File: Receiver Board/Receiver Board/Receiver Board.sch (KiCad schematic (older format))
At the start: 18 parts

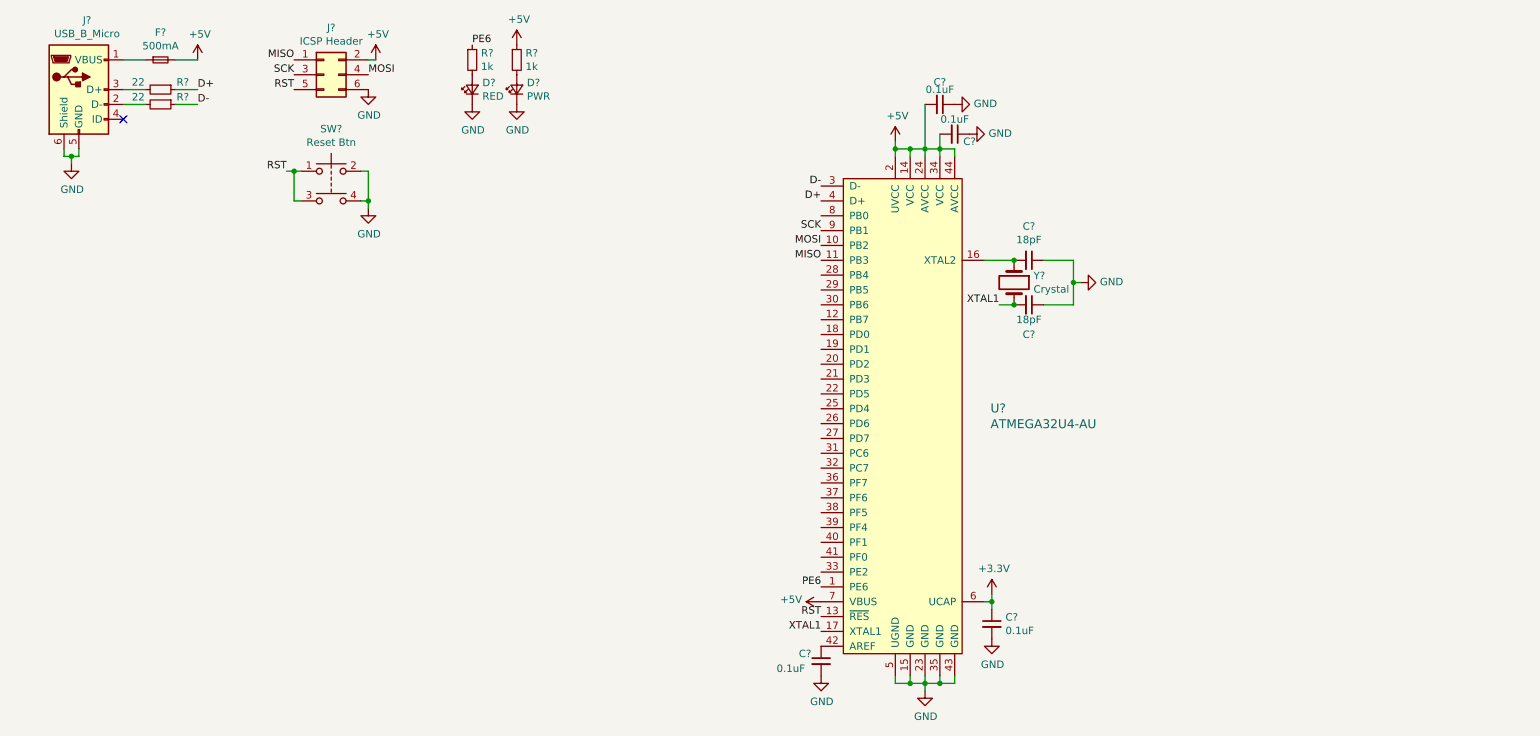
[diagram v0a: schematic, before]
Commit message: Receiver Board Schematic Complete
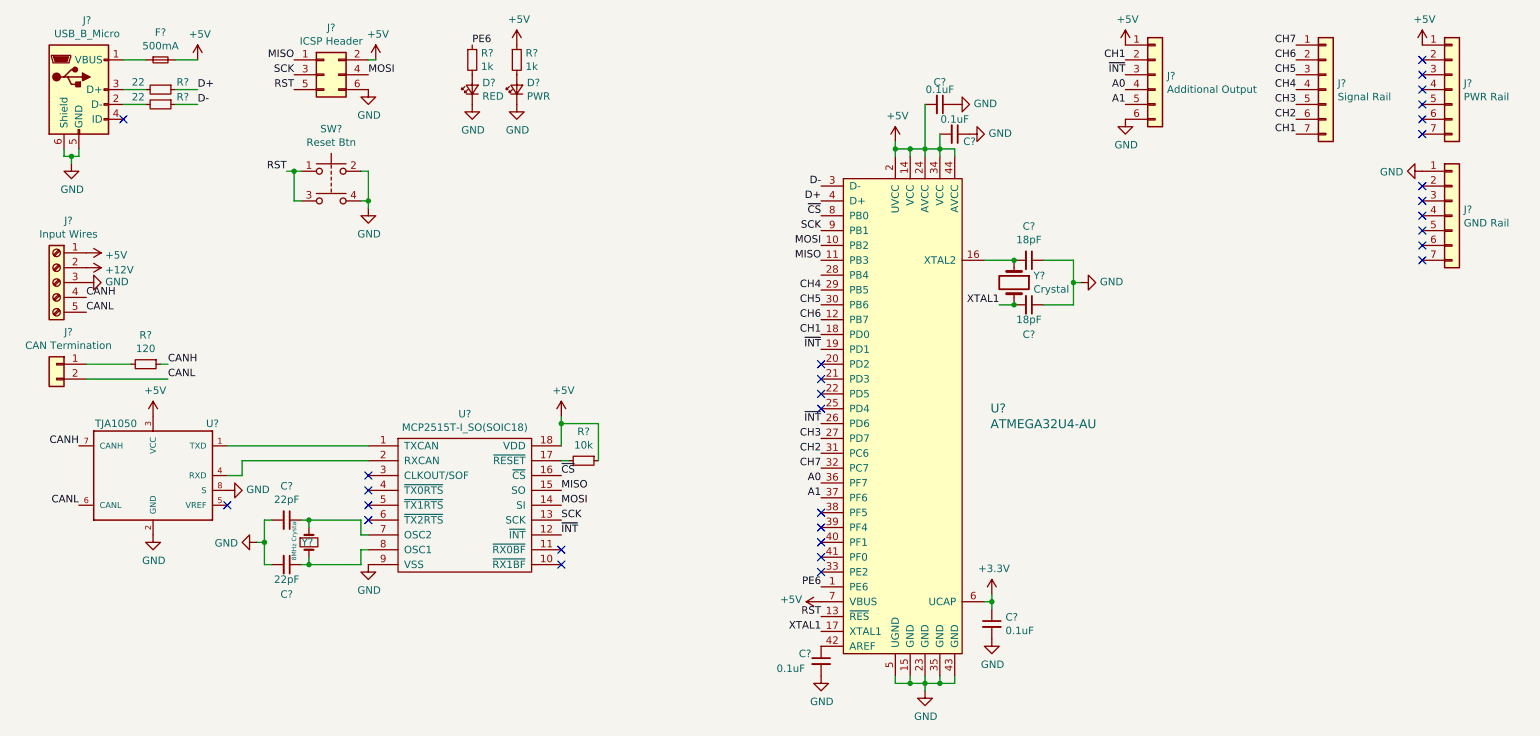
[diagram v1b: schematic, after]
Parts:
- added C? (x2): 22pF, symbol Device:C_Small
- added J?: Input Wires, symbol Connector:Screw_Terminal_01x05
- added J?: CAN Termination, symbol Connector_Generic:Conn_01x02
- added J?: Signal Rail, symbol Connector_Generic:Conn_01x07
- added J?: PWR Rail, symbol Connector_Generic:Conn_01x07
- added J?: GND Rail, symbol Connector_Generic:Conn_01x07
- added J?: Additional Output, symbol Connector_Generic:Conn_01x06
- added R?: 120, symbol Device:R_Small
- added R?: 10k, symbol Device:R_Small
- added U?: MCP2515T-I_SO(SOIC18), symbol Sailbot_Schematic_Symbols:MCP2515T-I_SO(SOIC18)
- added U?: TJA1050, symbol Sailbot_Schematic_Symbols:TJA1050
- added Y?: 8MHz Crystal, symbol Device:Crystal_Small
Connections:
- net +5V: now also J?.1 (Pin_1), J?.1 (Pin_1), J?.1 (Pin_1), R?.1, U?.18 (VDD), U?.3 (VCC)
- net GND: now also C?.2, C?.2, J?.1 (Pin_1), J?.3 (Pin_3), J?.6 (Pin_6), U?.2 (GND), U?.8 (S), U?.9 (VSS)
- net MISO: now also U?.15 (SO)
- net MOSI: now also U?.14 (SI)
- net SCK: now also U?.13 (SCK)
- net CH6: now reaches U?.12 (PB7)
- net CH6: now also J?.2 (Pin_2)
- net CH1: now reaches U?.18 (PD0)
- net CH1: now also J?.2 (Pin_2), J?.7 (Pin_7)
- net ~INT: now reaches U?.19 (PD1)
- net ~INT: now also U?.26 (PD6), J?.3 (Pin_3), U?.12 (~INT)
- net CH3: now reaches U?.27 (PD7)
- net CH3: now also J?.5 (Pin_5)
- net CH4: now reaches U?.29 (PB5)
- net CH4: now also J?.4 (Pin_4)
- net CH5: now reaches U?.30 (PB6)
- net CH5: now also J?.3 (Pin_3)
- net CH2: now reaches U?.31 (PC6)
- net CH2: now also J?.6 (Pin_6)
- net CH7: now reaches U?.32 (PC7)
- net CH7: now also J?.1 (Pin_1)
- net A0: now reaches U?.36 (PF7)
- net A0: now also J?.4 (Pin_4)
- net A1: now reaches U?.37 (PF6)
- net A1: now also J?.5 (Pin_5)
- net ~CS: now reaches U?.8 (PB0)
- net ~CS: now also U?.16 (~CS)
- new net: U?.1 (TXCAN), U?.1 (TXD)
- new net: R?.2, U?.17 (~RESET)
- new net: U?.2 (RXCAN), U?.4 (RXD)
- new net: C?.1, U?.7 (OSC2), Y?.1
- new net: C?.1, U?.8 (OSC1), Y?.2
- new net: J?.1 (Pin_1), R?.2
- new net +12V: J?.2 (Pin_2)
- new net CANH: J?.4 (Pin_4), R?.1, U?.7 (CANH)
- new net CANL: J?.2 (Pin_2), J?.5 (Pin_5), U?.6 (CANL)
- no-connect marks 1 -> 29

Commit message: Added master footprints library and updated footprint assignments for receiver board
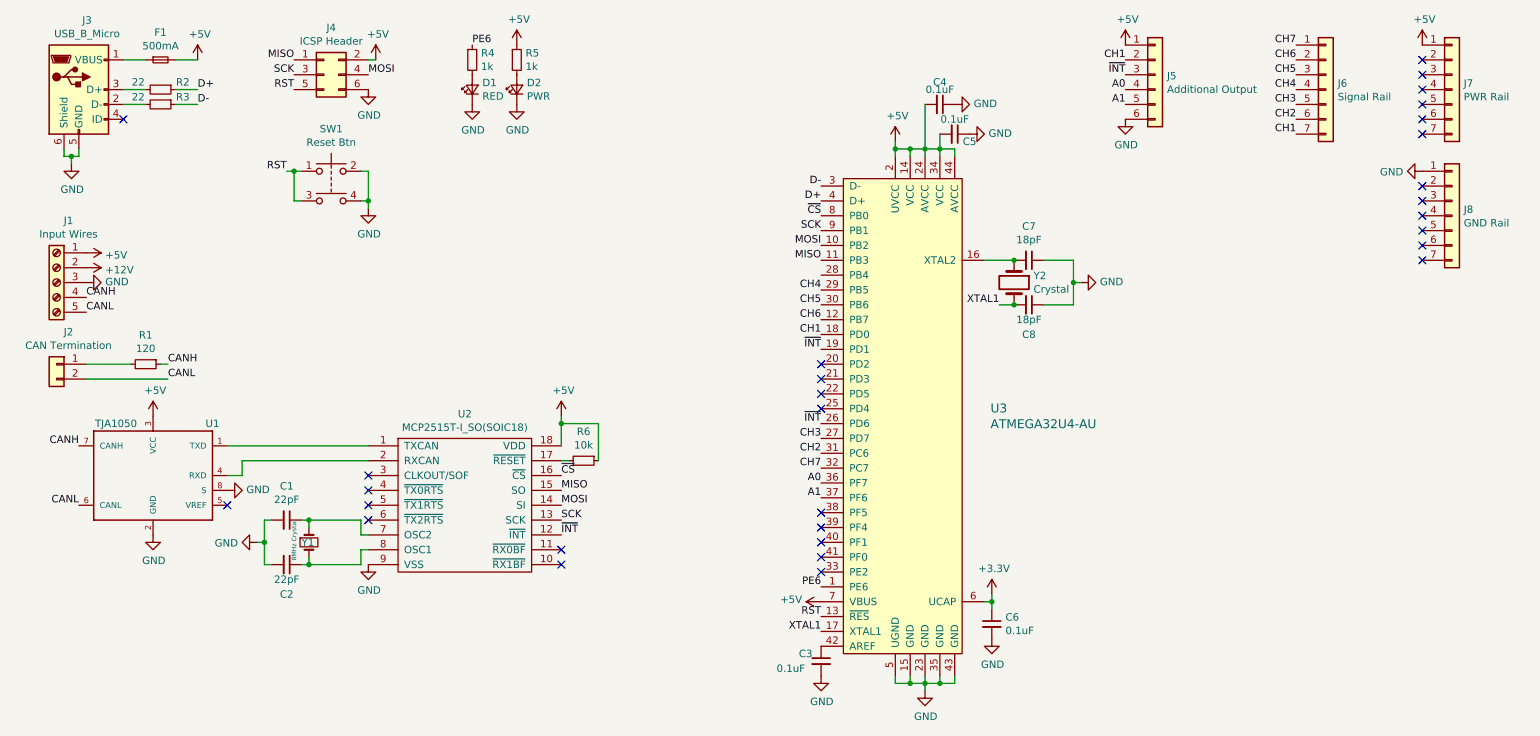
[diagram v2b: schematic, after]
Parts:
- C1, C2, C3, C4, C5, C6, C7, C8: renamed from C?; footprint (none) -> Capacitors_SMD:C_0603
- D1, D2: renamed from D?; footprint (none) -> Diodes_SMD:D_0603
- F1: renamed from F?; footprint (none) -> Fuse:Fuse_1812_4532Metric
- J1: renamed from J?; footprint (none) -> TerminalBlock_Phoenix:TerminalBlock_Phoenix_MKDS-1,5-5-5.08_1x05_P5.08mm_Horizontal
- J2: renamed from J?; footprint (none) -> Pin_Headers:Pin_Header_Straight_1x02_Pitch2.54mm
- J3: renamed from J?; footprint (none) -> Connector_USB:USB_Micro-B_Molex-105017-0001
- J4: renamed from J?; footprint (none) -> Pin_Headers:Pin_Header_Straight_2x03_Pitch2.54mm
- J5: renamed from J?; footprint (none) -> Connector_PinSocket_2.54mm:PinSocket_1x06_P2.54mm_Vertical
- J6, J7, J8: renamed from J?; footprint (none) -> Connector_PinSocket_2.54mm:PinSocket_1x07_P2.54mm_Vertical
- R1, R2, R3, R4, R5, R6: renamed from R?; footprint (none) -> Resistors_SMD:R_0603
- SW1: renamed from SW?; footprint (none) -> Button_Switch_SMD:SW_SPST_PTS645
- U1: renamed from U?; footprint (none) -> digikey-footprints:SOIC-8_W5.3mm
- U2: renamed from U?; footprint (none) -> digikey-footprints:SOIC-18_W7.5mm
- Y1, Y2: renamed from Y?; footprint (none) -> Crystals:Crystal_HC49-U_Vertical
- gave numbers to parts that had none: 1

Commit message: Board Design Prelim
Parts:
- removed SW1: Reset Btn, Button_Switch_SMD:SW_SPST_PTS645, symbol Switch:SW_Push_Dual
- added SW1: RESET BTN, Button_Switch_SMD:SW_SPST_PTS645, symbol Switch:SW_SPST
- C1, C2, C3, C4, C5, C6, C7, C8: footprint Capacitors_SMD:C_0603 -> Capacitor_SMD:C_0603_1608Metric
- D1, D2: footprint Diodes_SMD:D_0603 -> Diode_SMD:D_0603_1608Metric
- J2: footprint Pin_Headers:Pin_Header_Straight_1x02_Pitch2.54mm -> Connector_PinHeader_2.54mm:PinHeader_1x02_P2.54mm_Vertical
- J4: footprint Pin_Headers:Pin_Header_Straight_2x03_Pitch2.54mm -> Connector_PinHeader_2.54mm:PinHeader_2x03_P2.54mm_Vertical
- R1, R2, R3, R4, R5, R6: footprint Resistors_SMD:R_0603 -> Resistor_SMD:R_0603_1608Metric
- U1: symbol Sailbot_Schematic_Symbols:TJA1050 -> Receiver-Board-rescue:TJA1050-Sailbot_Schematic_Symbols
- U2: symbol Sailbot_Schematic_Symbols:MCP2515T-I_SO(SOIC18) -> Receiver-Board-rescue:MCP2515T-I_SO(SOIC18)-Sailbot_Schematic_Symbols
- Y1, Y2: footprint Crystals:Crystal_HC49-U_Vertical -> Crystal:Crystal_HC49-U_Vertical
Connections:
- net CANH: now also J1.5 (Pin_5); no longer J1.4 (Pin_4)
- net CANL: now also J1.4 (Pin_4); no longer J1.5 (Pin_5)
- net GND: now also SW1.2 (B)
- net RST: now also SW1.1 (A)
- net +3V3: no longer names the net of C6.1, U3.6 (UCAP)
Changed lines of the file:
@@
 F 0 "R2" V 1600 1400 50  0000 C CNN
 F 1 "22" V 1600 1100 50  0000 C CNN
-F 2 "Resistors_SMD:R_0603" H 1650 1250 50  0001 C CNN
+F 2 "Resistor_SMD:R_0603_1608Metric" H 1650 1250 50  0001 C CNN
 F 3 "~" H 1650 1250 50  0001 C CNN
 	1    1650 1250
@@
 F 0 "R3" V 1600 1500 50  0000 C CNN
 F 1 "22" V 1600 1200 50  0000 C CNN
-F 2 "Resistors_SMD:R_0603" H 1650 1350 50  0001 C CNN
+F 2 "Resistor_SMD:R_0603_1608Metric" H 1650 1350 50  0001 C CNN
 F 3 "~" H 1650 1350 50  0001 C CNN
 	1    1650 1350
@@
 F 0 "J4" H 2800 1467 50  0000 C CNN
 F 1 "ICSP Header" H 2800 1376 50  0000 C CNN
-F 2 "Pin_Headers:Pin_Header_Straight_2x03_Pitch2.54mm" H 2750 1150 50  0001 C CNN
+F 2 "Connector_PinHeader_2.54mm:PinHeader_2x03_P2.54mm_Vertical" H 2750 1150 50  0001 C CNN
 F 3 "~" H 2750 1150 50  0001 C CNN
 	1    2750 1150
@@
 F 0 "C5" V 7050 1650 50  0000 C CNN
 F 1 "0.1uF" V 6900 1550 50  0000 C CNN
-F 2 "Capacitors_SMD:C_0603" H 7000 1550 50  0001 C CNN
+F 2 "Capacitor_SMD:C_0603_1608Metric" H 7000 1550 50  0001 C CNN
 F 3 "~" H 7000 1550 50  0001 C CNN
 	1    7000 1550
@@
 F 0 "C4" V 6750 1350 50  0000 C CNN
 F 1 "0.1uF" V 6800 1350 50  0000 C CNN
-F 2 "Capacitors_SMD:C_0603" H 6900 1350 50  0001 C CNN
+F 2 "Capacitor_SMD:C_0603_1608Metric" H 6900 1350 50  0001 C CNN
 F 3 "~" H 6900 1350 50  0001 C CNN
 	1    6900 1350
@@
 F 0 "C6" H 7342 4896 50  0000 L CNN
 F 1 "0.1uF" H 7342 4805 50  0000 L CNN
-F 2 "Capacitors_SMD:C_0603" H 7250 4850 50  0001 C CNN
+F 2 "Capacitor_SMD:C_0603_1608Metric" H 7250 4850 50  0001 C CNN
 F 3 "~" H 7250 4850 50  0001 C CNN
 	1    7250 4850
@@
 $EndComp
 $Comp
-L power:+3.3V #PWR0107
-U 1 1 5D1C21C7
-P 7250 4650
-F 0 "#PWR0107" H 7250 4500 50  0001 C CNN
-F 1 "+3.3V" H 7265 4823 50  0000 C CNN
-F 2 "" H 7250 4650 50  0001 C CNN
-F 3 "" H 7250 4650 50  0001 C CNN
-	1    7250 4650
-	1    0    0    -1
-$EndComp
-Wire Wire Line
-	7250 4650 7250 4700
-Connection ~ 7250 4700
-$Comp
 L Device:Crystal Y2
 U 1 1 5D1C2677
@@
 F 0 "Y2" V 7354 2681 50  0000 L CNN
 F 1 "Crystal" V 7445 2681 50  0000 L CNN
-F 2 "Crystals:Crystal_HC49-U_Vertical" H 7400 2550 50  0001 C CNN
+F 2 "Crystal:Crystal_HC49-U_Vertical" H 7400 2550 50  0001 C CNN
 F 3 "~" H 7400 2550 50  0001 C CNN
 	1    7400 2550
@@
 F 0 "C7" V 7271 2400 50  0000 C CNN
 F 1 "18pF" V 7362 2400 50  0000 C CNN
-F 2 "Capacitors_SMD:C_0603" H 7500 2400 50  0001 C CNN
+F 2 "Capacitor_SMD:C_0603_1608Metric" H 7500 2400 50  0001 C CNN
 F 3 "~" H 7500 2400 50  0001 C CNN
 	1    7500 2400
@@
 F 0 "C8" V 7700 2700 50  0000 C CNN
 F 1 "18pF" V 7600 2700 50  0000 C CNN
-F 2 "Capacitors_SMD:C_0603" H 7500 2700 50  0001 C CNN
+F 2 "Capacitor_SMD:C_0603_1608Metric" H 7500 2700 50  0001 C CNN
 F 3 "~" H 7500 2700 50  0001 C CNN
 	1    7500 2700
@@
 F 0 "C3" H 5950 5150 50  0000 L CNN
 F 1 "0.1uF" H 5800 5050 50  0000 L CNN
-F 2 "Capacitors_SMD:C_0603" H 6100 5100 50  0001 C CNN
+F 2 "Capacitor_SMD:C_0603_1608Metric" H 6100 5100 50  0001 C CNN
 F 3 "~" H 6100 5100 50  0001 C CNN
 	1    6100 5100
@@
 F 0 "R4" H 3809 1096 50  0000 L CNN
 F 1 "1k" H 3809 1005 50  0000 L CNN
-F 2 "Resistors_SMD:R_0603" H 3750 1050 50  0001 C CNN
+F 2 "Resistor_SMD:R_0603_1608Metric" H 3750 1050 50  0001 C CNN
 F 3 "~" H 3750 1050 50  0001 C CNN
 	1    3750 1050
@@
 F 0 "D1" V 3796 1182 50  0000 R CNN
 F 1 "RED" V 3705 1182 50  0000 R CNN
-F 2 "Diodes_SMD:D_0603" V 3750 1250 50  0001 C CNN
+F 2 "Diode_SMD:D_0603_1608Metric" V 3750 1250 50  0001 C CNN
 F 3 "~" V 3750 1250 50  0001 C CNN
 	1    3750 1250
@@
 $EndComp
 $Comp
-L Switch:SW_Push_Dual SW1
-U 1 1 5D1CA4A0
-P 2800 1800
-F 0 "SW1" H 2800 2085 50  0000 C CNN
-F 1 "Reset Btn" H 2800 1994 50  0000 C CNN
-F 2 "Button_Switch_SMD:SW_SPST_PTS645" H 2800 2000 50  0001 C CNN
-F 3 "" H 2800 2000 50  0001 C CNN
-	1    2800 1800
-	1    0    0    -1
-$EndComp
-$Comp
 L power:GND #PWR0115
 U 1 1 5D1CA576
-P 3050 2050
-F 0 "#PWR0115" H 3050 1800 50  0001 C CNN
-F 1 "GND" H 3055 1877 50  0000 C CNN
-F 2 "" H 3050 2050 50  0001 C CNN
-F 3 "" H 3050 2050 50  0001 C CNN
-	1    3050 2050
-	1    0    0    -1
-$EndComp
-Wire Wire Line
-	3000 2000 3050 2000
-Wire Wire Line
-	3050 2000 3050 2050
-Wire Wire Line
-	3050 2000 3050 1800
-Wire Wire Line
-	3050 1800 3000 1800
-Connection ~ 3050 2000
+P 3000 1800
+F 0 "#PWR0115" H 3000 1550 50  0001 C CNN
+F 1 "GND" H 3005 1627 50  0000 C CNN
+F 2 "" H 3000 1800 50  0001 C CNN
+F 3 "" H 3000 1800 50  0001 C CNN
+	1    3000 1800
+	0    -1   -1   0
+$EndComp
 Text Label 2500 1800 2    50   ~ 0
 RST
-Wire Wire Line
-	2550 1800 2550 2000
-Wire Wire Line
-	2550 2000 2600 2000
-Wire Wire Line
-	2600 1800 2550 1800
-Wire Wire Line
-	2500 1800 2550 1800
-Connection ~ 2550 1800
 $Comp
 L Device:R_Small R5
@@
 F 0 "R5" H 4109 1096 50  0000 L CNN
 F 1 "1k" H 4109 1005 50  0000 L CNN
-F 2 "Resistors_SMD:R_0603" H 4050 1050 50  0001 C CNN
+F 2 "Resistor_SMD:R_0603_1608Metric" H 4050 1050 50  0001 C CNN
 F 3 "~" H 4050 1050 50  0001 C CNN
 	1    4050 1050
@@
 F 0 "D2" V 4096 1182 50  0000 R CNN
 F 1 "PWR" V 4005 1182 50  0000 R CNN
-F 2 "Diodes_SMD:D_0603" V 4050 1250 50  0001 C CNN
+F 2 "Diode_SMD:D_0603_1608Metric" V 4050 1250 50  0001 C CNN
 F 3 "~" V 4050 1250 50  0001 C CNN
 	1    4050 1250
@@
 $EndComp
 $Comp
-L Sailbot_Schematic_Symbols:MCP2515T-I_SO(SOIC18) U2
+L Receiver-Board-rescue:MCP2515T-I_SO(SOIC18)-Sailbot_Schematic_Symbols U2
 U 1 1 5D1D1D38
 P 3700 4100
@@
 $EndComp
 $Comp
-L Sailbot_Schematic_Symbols:TJA1050 U1
+L Receiver-Board-rescue:TJA1050-Sailbot_Schematic_Symbols U1
 U 1 1 5D1D1DCD
 P 1600 3850
@@
 F 0 "J2" H 870 3317 50  0000 C CNN
 F 1 "CAN Termination" H 870 3226 50  0000 C CNN
-F 2 "Pin_Headers:Pin_Header_Straight_1x02_Pitch2.54mm" H 950 3100 50  0001 C CNN
+F 2 "Connector_PinHeader_2.54mm:PinHeader_1x02_P2.54mm_Vertical" H 950 3100 50  0001 C CNN
 F 3 "~" H 950 3100 50  0001 C CNN
 	1    950  3100
@@
 F 0 "R1" V 1354 3100 50  0000 C CNN
 F 1 "120" V 1445 3100 50  0000 C CNN
-F 2 "Resistors_SMD:R_0603" H 1550 3100 50  0001 C CNN
+F 2 "Resistor_SMD:R_0603_1608Metric" H 1550 3100 50  0001 C CNN
 F 3 "~" H 1550 3100 50  0001 C CNN
 	1    1550 3100
@@
 Text Label 1700 3200 0    50   ~ 0
 CANL
+Text Label 1150 2750 0    50   ~ 0
+CANH
 Text Label 1150 2650 0    50   ~ 0
-CANH
-Text Label 1150 2750 0    50   ~ 0
 CANL
 Text Label 1100 3650 2    50   ~ 0
@@
 F 0 "R6" V 4304 3750 50  0000 C CNN
 F 1 "10k" V 4395 3750 50  0000 C CNN
-F 2 "Resistors_SMD:R_0603" H 4500 3750 50  0001 C CNN
+F 2 "Resistor_SMD:R_0603_1608Metric" H 4500 3750 50  0001 C CNN
 F 3 "~" H 4500 3750 50  0001 C CNN
 	1    4500 3750
@@
 F 0 "Y1" V 2650 4250 50  0000 L CNN
 F 1 "8MHz Crystal" H 2500 4200 30  0000 L CNN
-F 2 "Crystals:Crystal_HC49-U_Vertical" H 2650 4300 50  0001 C CNN
+F 2 "Crystal:Crystal_HC49-U_Vertical" H 2650 4300 50  0001 C CNN
 F 3 "~" H 2650 4300 50  0001 C CNN
 	1    2650 4300
@@
 F 0 "C1" V 2271 4150 50  0000 C CNN
 F 1 "22pF" V 2362 4150 50  0000 C CNN
-F 2 "Capacitors_SMD:C_0603" H 2500 4150 50  0001 C CNN
+F 2 "Capacitor_SMD:C_0603_1608Metric" H 2500 4150 50  0001 C CNN
 F 3 "~" H 2500 4150 50  0001 C CNN
 	1    2500 4150
@@
 F 0 "C2" V 2700 4450 50  0000 C CNN
 F 1 "22pF" V 2600 4450 50  0000 C CNN
-F 2 "Capacitors_SMD:C_0603" H 2500 4450 50  0001 C CNN
+F 2 "Capacitor_SMD:C_0603_1608Metric" H 2500 4450 50  0001 C CNN
 F 3 "~" H 2500 4450 50  0001 C CNN
 	1    2500 4450
@@
 NoConn ~ 6100 3200
 NoConn ~ 6100 3100
+$Comp
+L Switch:SW_SPST SW1
+U 1 1 5D1D7B60
+P 2800 1800
+F 0 "SW1" H 2800 2035 50  0000 C CNN
+F 1 "RESET BTN" H 2800 1944 50  0000 C CNN
+F 2 "Button_Switch_SMD:SW_SPST_PTS645" H 2800 1800 50  0001 C CNN
+F 3 "" H 2800 1800 50  0001 C CNN
+	1    2800 1800
+	1    0    0    -1
+$EndComp
+Wire Wire Line
+	2500 1800 2600 1800
 $EndSCHEMATC
